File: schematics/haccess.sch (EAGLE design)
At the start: 34 parts, among them Q1 BSS123, SW1 SPST_TACT, SW2 SPST_TACT, U1 MCP2300X/SO, U2 ESP826607B, U3 OPTOISOLATOR-2SOIC8

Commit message: Changed backlight to use 0805 pads - still usable with 0603 parts, but easier to solder
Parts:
- BL1, BL2, BL3: device led:LEDCHIPLED_0603 -> led:LEDCHIP-LED0805
- BL4: device led:LEDCHIPLED_0603 -> led:LEDCHIPLED_0805
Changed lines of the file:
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@@
 <grid distance="0.1" unitdist="inch" unit="inch" style="lines" multiple="1" display="no" altdistance="0.01" altunitdist="inch" altunit="inch"/>
 <layers>
-<layer number="1" name="Top" color="4" fill="1" visible="no" active="no"/>
-<layer number="2" name="Route2" color="1" fill="3" visible="no" active="no"/>
-<layer number="3" name="Route3" color="4" fill="3" visible="no" active="no"/>
-<layer number="4" name="Route4" color="1" fill="4" visible="no" active="no"/>
-<layer number="5" name="Route5" color="4" fill="4" visible="no" active="no"/>
-<layer number="6" name="Route6" color="1" fill="8" visible="no" active="no"/>
-<layer number="7" name="Route7" color="4" fill="8" visible="no" active="no"/>
-<layer number="8" name="Route8" color="1" fill="2" visible="no" active="no"/>
-<layer number="9" name="Route9" color="4" fill="2" visible="no" active="no"/>
-<layer number="10" name="Route10" color="1" fill="7" visible="no" active="no"/>
-<layer number="11" name="Route11" color="4" fill="7" visible="no" active="no"/>
-<layer number="12" name="Route12" color="1" fill="5" visible="no" active="no"/>
-<layer number="13" name="Route13" color="4" fill="5" visible="no" active="no"/>
-<layer number="14" name="Route14" color="1" fill="6" visible="no" active="no"/>
-<layer number="15" name="Route15" color="4" fill="6" visible="no" active="no"/>
-<layer number="16" name="Bottom" color="1" fill="1" visible="no" active="no"/>
-<layer number="17" name="Pads" color="2" fill="1" visible="no" active="no"/>
-<layer number="18" name="Vias" color="2" fill="1" visible="no" active="no"/>
-<layer number="19" name="Unrouted" color="6" fill="1" visible="no" active="no"/>
-<layer number="20" name="Dimension" color="15" fill="1" visible="no" active="no"/>
-<layer number="21" name="tPlace" color="7" fill="1" visible="no" active="no"/>
-<layer number="22" name="bPlace" color="7" fill="1" visible="no" active="no"/>
-<layer number="23" name="tOrigins" color="15" fill="1" visible="no" active="no"/>
-<layer number="24" name="bOrigins" color="15" fill="1" visible="no" active="no"/>
-<layer number="25" name="tNames" color="7" fill="1" visible="no" active="no"/>
-<layer number="26" name="bNames" color="7" fill="1" visible="no" active="no"/>
-<layer number="27" name="tValues" color="7" fill="1" visible="no" active="no"/>
-<layer number="28" name="bValues" color="7" fill="1" visible="no" active="no"/>
+<layer number="1" name="Top" color="4" fill="1" visible="yes" active="no"/>
+<layer number="2" name="Route2" color="1" fill="3" visible="yes" active="no"/>
+<layer number="3" name="Route3" color="4" fill="3" visible="yes" active="no"/>
+<layer number="4" name="Route4" color="1" fill="4" visible="yes" active="no"/>
+<layer number="5" name="Route5" color="4" fill="4" visible="yes" active="no"/>
+<layer number="6" name="Route6" color="1" fill="8" visible="yes" active="no"/>
+<layer number="7" name="Route7" color="4" fill="8" visible="yes" active="no"/>
+<layer number="8" name="Route8" color="1" fill="2" visible="yes" active="no"/>
+<layer number="9" name="Route9" color="4" fill="2" visible="yes" active="no"/>
+<layer number="10" name="Route10" color="1" fill="7" visible="yes" active="no"/>
+<layer number="11" name="Route11" color="4" fill="7" visible="yes" active="no"/>
+<layer number="12" name="Route12" color="1" fill="5" visible="yes" active="no"/>
+<layer number="13" name="Route13" color="4" fill="5" visible="yes" active="no"/>
+<layer number="14" name="Route14" color="1" fill="6" visible="yes" active="no"/>
+<layer number="15" name="Route15" color="4" fill="6" visible="yes" active="no"/>
+<layer number="16" name="Bottom" color="1" fill="1" visible="yes" active="no"/>
+<layer number="17" name="Pads" color="2" fill="1" visible="yes" active="no"/>
+<layer number="18" name="Vias" color="2" fill="1" visible="yes" active="no"/>
+<layer number="19" name="Unrouted" color="6" fill="1" visible="yes" active="no"/>
+<layer number="20" name="Dimension" color="15" fill="1" visible="yes" active="no"/>
+<layer number="21" name="tPlace" color="7" fill="1" visible="yes" active="no"/>
+<layer number="22" name="bPlace" color="7" fill="1" visible="yes" active="no"/>
+<layer number="23" name="tOrigins" color="15" fill="1" visible="yes" active="no"/>
+<layer number="24" name="bOrigins" color="15" fill="1" visible="yes" active="no"/>
+<layer number="25" name="tNames" color="7" fill="1" visible="yes" active="no"/>
+<layer number="26" name="bNames" color="7" fill="1" visible="yes" active="no"/>
+<layer number="27" name="tValues" color="7" fill="1" visible="yes" active="no"/>
+<layer number="28" name="bValues" color="7" fill="1" visible="yes" active="no"/>
 <layer number="29" name="tStop" color="7" fill="3" visible="no" active="no"/>
 <layer number="30" name="bStop" color="7" fill="6" visible="no" active="no"/>
@@
 <layer number="35" name="tGlue" color="7" fill="4" visible="no" active="no"/>
 <layer number="36" name="bGlue" color="7" fill="5" visible="no" active="no"/>
-<layer number="37" name="tTest" color="7" fill="1" visible="no" active="no"/>
-<layer number="38" name="bTest" color="7" fill="1" visible="no" active="no"/>
+<layer number="37" name="tTest" color="7" fill="1" visible="yes" active="no"/>
+<layer number="38" name="bTest" color="7" fill="1" visible="yes" active="no"/>
 <layer number="39" name="tKeepout" color="4" fill="11" visible="no" active="no"/>
 <layer number="40" name="bKeepout" color="1" fill="11" visible="no" active="no"/>
@@
 <layer number="44" name="Drills" color="7" fill="1" visible="no" active="no"/>
 <layer number="45" name="Holes" color="7" fill="1" visible="no" active="no"/>
-<layer number="46" name="Milling" color="3" fill="1" visible="no" active="no"/>
-<layer number="47" name="Measures" color="7" fill="1" visible="no" active="no"/>
-<layer number="48" name="Document" color="7" fill="1" visible="no" active="no"/>
-<layer number="49" name="Reference" color="7" fill="1" visible="no" active="no"/>
-<layer number="50" name="dxf" color="7" fill="1" visible="no" active="no"/>
-<layer number="51" name="tDocu" color="7" fill="1" visible="no" active="no"/>
-<layer number="52" name="bDocu" color="7" fill="1" visible="no" active="no"/>
-<layer number="53" name="tGND_GNDA" color="7" fill="9" visible="no" active="no"/>
-<layer number="54" name="bGND_GNDA" color="1" fill="9" visible="no" active="no"/>
-<layer number="56" name="wert" color="7" fill="1" visible="no" active="no"/>
-<layer number="57" name="tCAD" color="7" fill="1" visible="no" active="no"/>
+<layer number="46" name="Milling" color="3" fill="1" visible="yes" active="no"/>
+<layer number="47" name="Measures" color="7" fill="1" visible="yes" active="no"/>
+<layer number="48" name="Document" color="7" fill="1" visible="yes" active="no"/>
+<layer number="49" name="Reference" color="7" fill="1" visible="yes" active="no"/>
+<layer number="50" name="dxf" color="7" fill="1" visible="yes" active="no"/>
+<layer number="51" name="tDocu" color="7" fill="1" visible="yes" active="no"/>
+<layer number="52" name="bDocu" color="7" fill="1" visible="yes" active="no"/>
+<layer number="53" name="tGND_GNDA" color="7" fill="9" visible="yes" active="no"/>
+<layer number="54" name="bGND_GNDA" color="1" fill="9" visible="yes" active="no"/>
+<layer number="56" name="wert" color="7" fill="1" visible="yes" active="no"/>
+<layer number="57" name="tCAD" color="7" fill="1" visible="yes" active="no"/>
 <layer number="90" name="Modules" color="5" fill="1" visible="yes" active="yes"/>
 <layer number="91" name="Nets" color="2" fill="1" visible="yes" active="yes"/>
@@
 <part name="GND8" library="supply1" deviceset="GND" device=""/>
 <part name="GND9" library="supply1" deviceset="GND" device=""/>
-<part name="BL1" library="led" deviceset="LED" device="CHIPLED_0603"/>
+<part name="BL1" library="led" deviceset="LED" device="CHIP-LED0805"/>
 <part name="R3" library="rcl" deviceset="R-EU_" device="R0603" value="22R"/>
-<part name="BL2" library="led" deviceset="LED" device="CHIPLED_0603"/>
-<part name="BL3" library="led" deviceset="LED" device="CHIPLED_0603"/>
-<part name="BL4" library="led" deviceset="LED" device="CHIPLED_0603"/>
+<part name="BL2" library="led" deviceset="LED" device="CHIP-LED0805"/>
+<part name="BL3" library="led" deviceset="LED" device="CHIP-LED0805"/>
+<part name="BL4" library="led" deviceset="LED" device="CHIPLED_0805"/>
 <part name="+3V10" library="supply1" deviceset="+3V3" device=""/>
 <part name="+3V9" library="supply1" deviceset="+3V3" device=""/>

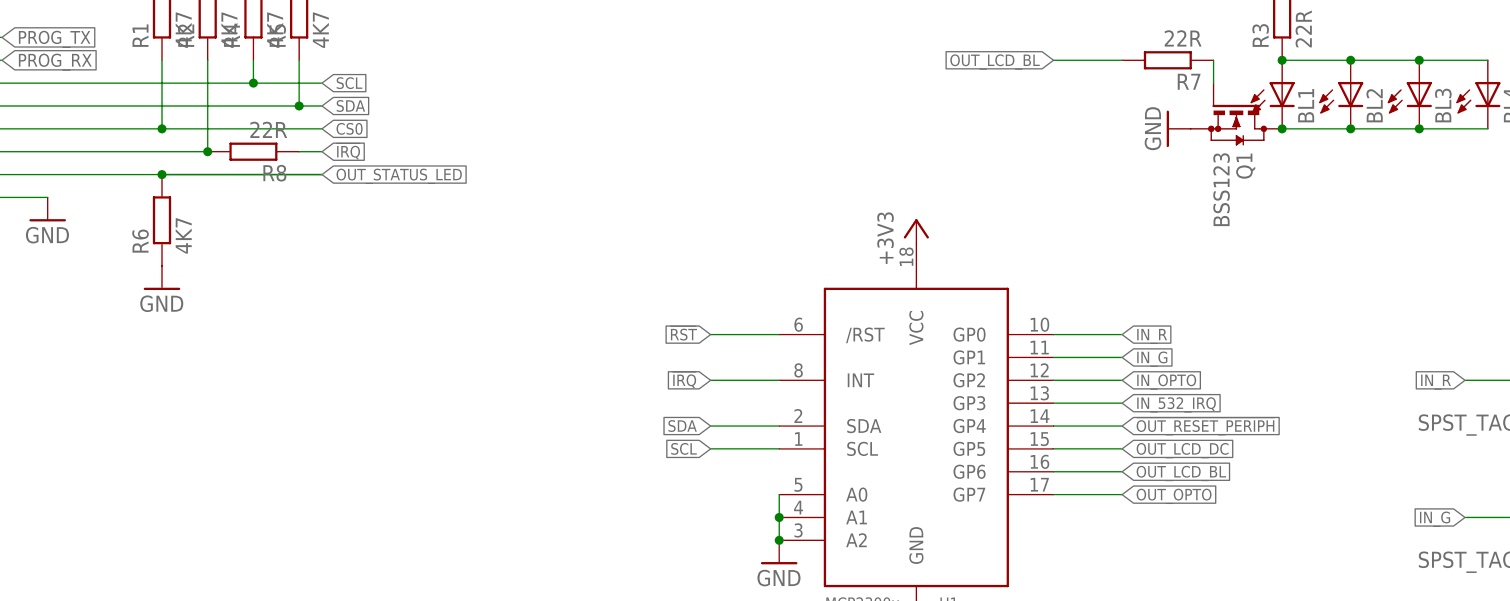
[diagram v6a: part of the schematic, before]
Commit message: Moved Status LED onto pin expander, i2c and LCD reset pins onto pin 15
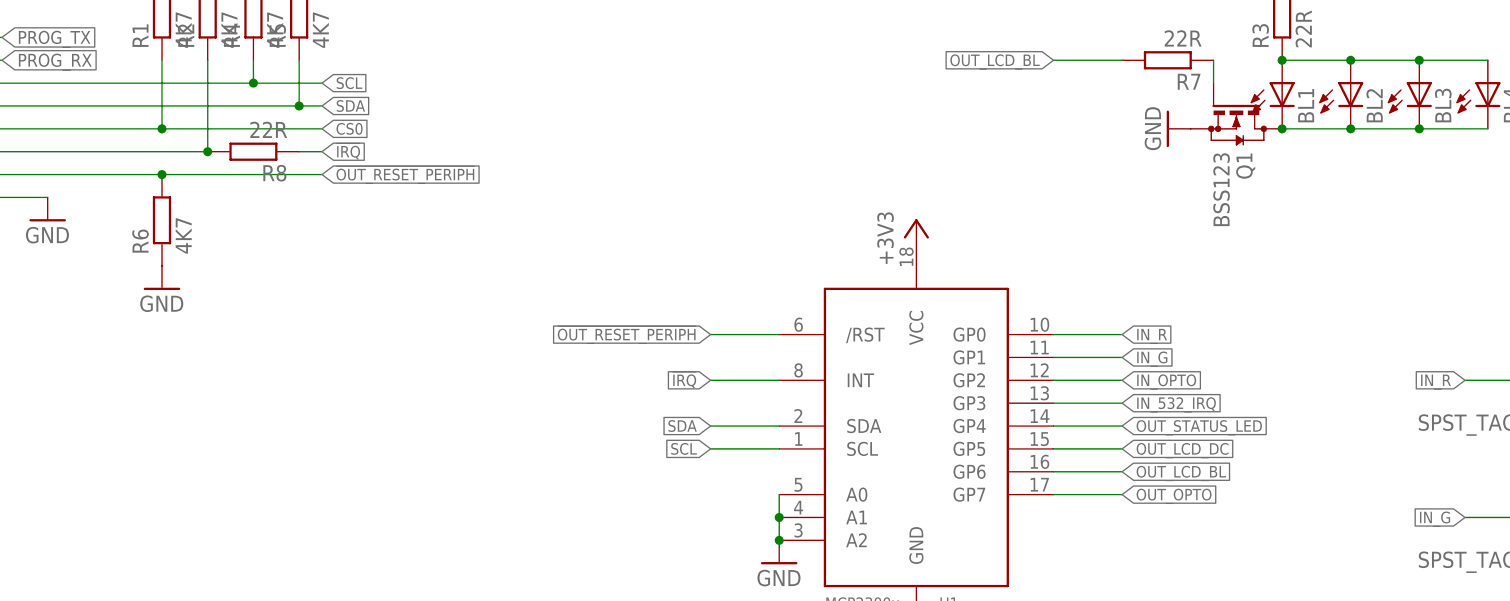
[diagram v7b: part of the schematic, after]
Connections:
- removed net !RST: U1./RST
- net !OUT_RESET_PERIPH: now also R6.2, U1./RST, U2.15; no longer U1.GP4
- net OUT_STATUS_LED: now also U1.GP4; no longer R6.2, U2.15
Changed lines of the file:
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@@
-</segment>
-</net>
-<net name="!RST" class="0">
-<segment>
-<pinref part="U1" gate="G$1" pin="/RST"/>
-<wire x1="111.76" y1="134.62" x2="104.14" y2="134.62" width="0.1524" layer="91"/>
-<label x="104.14" y="134.62" size="1.27" layer="95" rot="R180" xref="yes"/>
 </segment>
 </net>
@@
 <net name="!OUT_RESET_PERIPH" class="0">
 <segment>
-<pinref part="U1" gate="G$1" pin="GP4"/>
-<wire x1="142.24" y1="124.46" x2="149.86" y2="124.46" width="0.1524" layer="91"/>
-<label x="149.86" y="124.46" size="1.27" layer="95" xref="yes"/>
-</segment>
-<segment>
 <pinref part="LCD1" gate="G$1" pin="/RES"/>
 <wire x1="71.12" y1="73.66" x2="63.5" y2="73.66" width="0.1524" layer="91"/>
 <label x="63.5" y="73.66" size="1.27" layer="95" rot="R180" xref="yes"/>
+</segment>
+<segment>
+<pinref part="U2" gate="G$1" pin="15"/>
+<wire x1="22.86" y1="152.4" x2="43.18" y2="152.4" width="0.1524" layer="91"/>
+<label x="60.96" y="152.4" size="1.27" layer="95" xref="yes"/>
+<pinref part="R6" gate="G$1" pin="2"/>
+<wire x1="43.18" y1="152.4" x2="60.96" y2="152.4" width="0.1524" layer="91"/>
+<junction x="43.18" y="152.4"/>
+</segment>
+<segment>
+<pinref part="U1" gate="G$1" pin="/RST"/>
+<wire x1="111.76" y1="134.62" x2="104.14" y2="134.62" width="0.1524" layer="91"/>
+<label x="104.14" y="134.62" size="1.27" layer="95" rot="R180" xref="yes"/>
 </segment>
 </net>
@@
 </segment>
 <segment>
-<pinref part="U2" gate="G$1" pin="15"/>
-<wire x1="22.86" y1="152.4" x2="43.18" y2="152.4" width="0.1524" layer="91"/>
-<label x="60.96" y="152.4" size="1.27" layer="95" xref="yes"/>
-<pinref part="R6" gate="G$1" pin="2"/>
-<wire x1="43.18" y1="152.4" x2="60.96" y2="152.4" width="0.1524" layer="91"/>
-<junction x="43.18" y="152.4"/>
-<wire x1="43.18" y1="152.4" x2="60.96" y2="152.4" width="0.1524" layer="91"/>
+<pinref part="U1" gate="G$1" pin="GP4"/>
+<wire x1="142.24" y1="124.46" x2="149.86" y2="124.46" width="0.1524" layer="91"/>
+<label x="149.86" y="124.46" size="1.27" layer="95" xref="yes"/>
 </segment>
 </net>

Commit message: Increased status LED track sizes, changed 0805 leds to consistent package
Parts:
- BL1, BL2, BL3: device led:LEDCHIP-LED0805 -> led:LEDCHIPLED_0805
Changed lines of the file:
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@@
 <part name="GND8" library="supply1" deviceset="GND" device=""/>
 <part name="GND9" library="supply1" deviceset="GND" device=""/>
-<part name="BL1" library="led" deviceset="LED" device="CHIP-LED0805"/>
+<part name="BL1" library="led" deviceset="LED" device="CHIPLED_0805"/>
 <part name="R3" library="rcl" deviceset="R-EU_" device="R0603" value="22R"/>
-<part name="BL2" library="led" deviceset="LED" device="CHIP-LED0805"/>
-<part name="BL3" library="led" deviceset="LED" device="CHIP-LED0805"/>
+<part name="BL2" library="led" deviceset="LED" device="CHIPLED_0805"/>
+<part name="BL3" library="led" deviceset="LED" device="CHIPLED_0805"/>
 <part name="BL4" library="led" deviceset="LED" device="CHIPLED_0805"/>
 <part name="+3V10" library="supply1" deviceset="+3V3" device=""/>
@@
 </segment>
 </net>
-<net name="OUT_STATUS_LED" class="0">
+<net name="OUT_STATUS_LED" class="1">
 <segment>
 <pinref part="STATUS" gate="G$1" pin="C"/>
@@
 </segment>
 </net>
-<net name="N$2" class="0">
+<net name="N$2" class="1">
 <segment>
 <pinref part="STATUS" gate="G$1" pin="A"/>
